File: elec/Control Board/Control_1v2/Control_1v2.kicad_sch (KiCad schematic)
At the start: 163 parts, among them J1 DB9_Female_MountingHoles, J10 Conn_02x12_Odd_Even, J11 Screw_Terminal_01x02, J14 Conn_01x10, J2 Conn_01x08, J25 Screw_Terminal_01x02, J26 Conn_01x10, J27 Conn_02x12_Odd_Even, J28 Screw_Terminal_01x02, J29 Conn_01x10, J3 Conn_01x08, J37 Conn_01x04, J4 Conn_01x08, J5 Conn_01x08, J6 Conn_01x08, J7 Conn_01x10, J8 Conn_02x18_Odd_Even, J9 Conn_01x10, Q601 BSS138

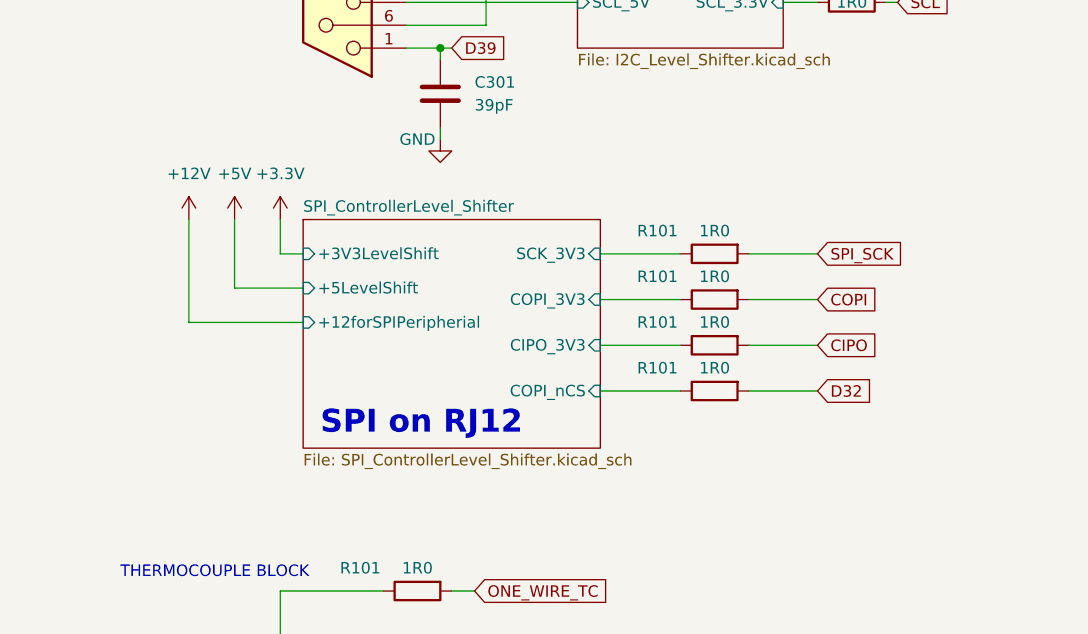
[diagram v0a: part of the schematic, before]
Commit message: Contrl 1.2 schematic, fix for Issue control board V1 kills ethernet boards #66
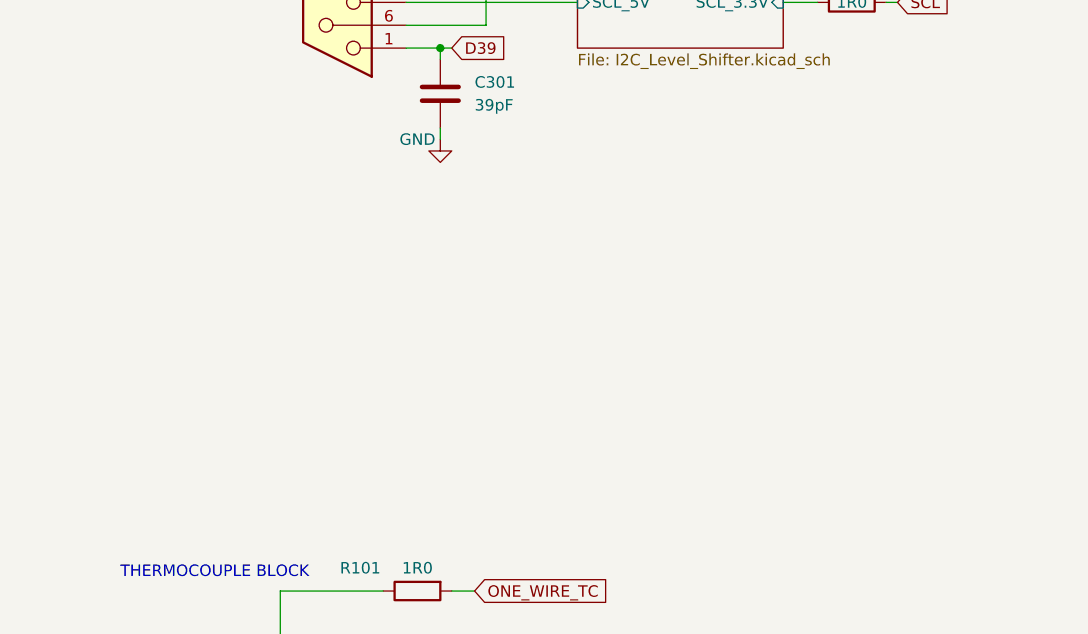
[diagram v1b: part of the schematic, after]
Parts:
- removed R101 (x4): 1R0, Resistor_SMD:R_0603_1608Metric_Pad0.98x0.95mm_HandSolder, symbol Device:R
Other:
- removed sheet SPI_ControllerLevel_Shifter
- note removed: "SPI on RJ12"

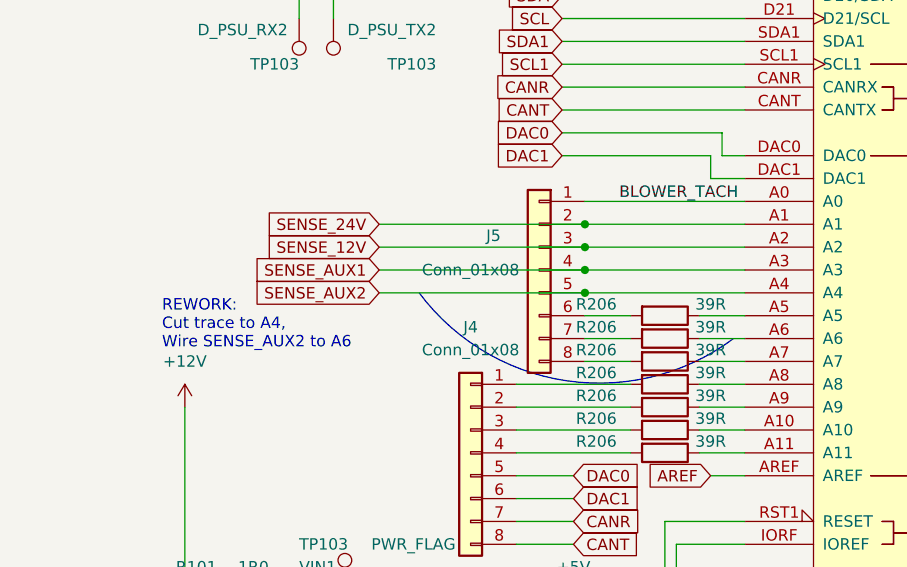
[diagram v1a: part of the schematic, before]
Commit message: Contrl 1.2 schematic, fix for Issue Control V1.1, A4 SENSE_AUX2 Conflicts With LAN Card SDA ( So does A5) #116
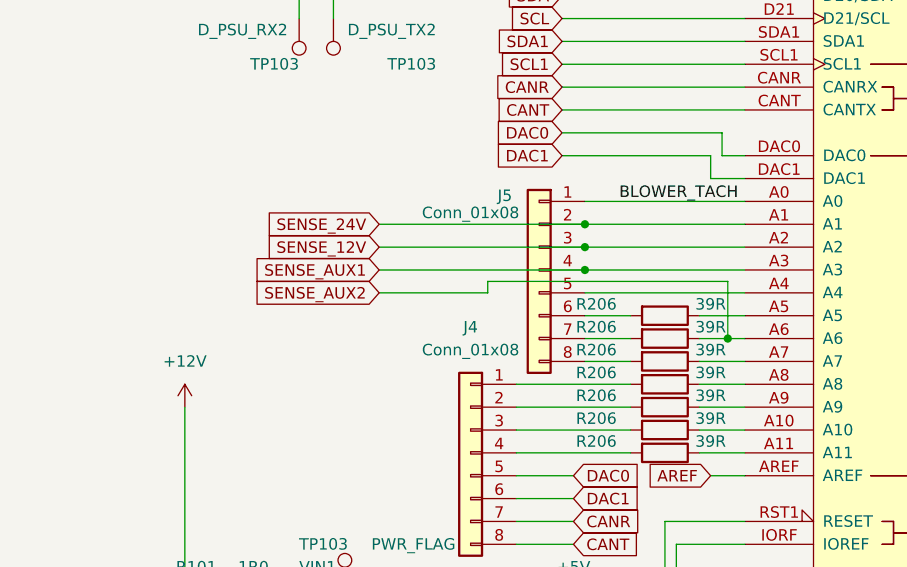
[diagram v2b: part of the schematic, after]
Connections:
- net SENSE_AUX2: now also A1.A6, R206.1; no longer A1.A4, J5.5 (Pin_5)
- new net: A1.A4, J5.5 (Pin_5)
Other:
- note removed: "REWORK: Cut trace to A4, Wire SENSE_AUX2 to A6"
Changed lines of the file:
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@@
   (junction (at 172.72 152.4) (diameter 0) (color 0 0 0 0)
   )
+  (junction (at 215.265 124.46) (diameter 0) (color 0 0 0 0)
+  )
   (junction (at 433.07 129.54) (diameter 0) (color 0 0 0 0)
   )
@@
   (junction (at 433.07 49.53) (diameter 0) (color 0 0 0 0)
   )
-  (junction (at 199.39 119.38) (diameter 0) (color 0 0 0 0)
-  )
   (junction (at 297.18 165.1) (diameter 0) (color 0 0 0 0)
   )
@@
     (stroke (width 0) (type default))
   )
+  (wire (pts (xy 215.265 124.46) (xy 217.17 124.46))
+    (stroke (width 0) (type default))
+  )
   (wire (pts (xy 463.55 148.59) (xy 463.55 134.62))
     (stroke (width 0) (type default))
@@
     (stroke (width 0) (type default))
   )
-  (wire (pts (xy 212.09 124.46) (xy 217.17 124.46))
-    (stroke (width 0) (type default))
-  )
   (wire (pts (xy 431.8 40.64) (xy 424.18 40.64))
     (stroke (width 0) (type default))
@@
     (stroke (width 0) (type default))
   )
+  (wire (pts (xy 188.595 118.11) (xy 188.595 119.38))
+    (stroke (width 0) (type default))
+  )
   (wire (pts (xy 307.34 139.7) (xy 317.5 139.7))
     (stroke (width 0) (type default))
@@
     (stroke (width 0) (type default))
   )
+  (wire (pts (xy 188.595 119.38) (xy 176.53 119.38))
+    (stroke (width 0) (type default))
+  )
   (wire (pts (xy 204.47 162.56) (xy 217.17 162.56))
     (stroke (width 0) (type default))
@@
     (stroke (width 0) (type default))
   )
+  (wire (pts (xy 212.09 124.46) (xy 215.265 124.46))
+    (stroke (width 0) (type default))
+  )
   (wire (pts (xy 488.95 261.62) (xy 494.03 261.62))
     (stroke (width 0) (type default))
@@
     (stroke (width 0) (type default))
   )
-  (wire (pts (xy 176.53 119.38) (xy 199.39 119.38))
-    (stroke (width 0) (type default))
-  )
   (wire (pts (xy 354.33 217.17) (xy 358.14 217.17))
     (stroke (width 0) (type default))
@@
     (stroke (width 0) (type default))
   )
+  (wire (pts (xy 199.39 124.46) (xy 204.47 124.46))
+    (stroke (width 0) (type default))
+  )
   (wire (pts (xy 199.39 119.38) (xy 217.17 119.38))
     (stroke (width 0) (type default))
@@
     (stroke (width 0) (type default))
   )
+  (wire (pts (xy 215.265 118.11) (xy 188.595 118.11))
+    (stroke (width 0) (type default))
+  )
   (wire (pts (xy 60.96 170.815) (xy 41.91 170.815))
     (stroke (width 0) (type default))
@@
     (stroke (width 0) (type default))
   )
+  (wire (pts (xy 215.265 124.46) (xy 215.265 118.11))
+    (stroke (width 0) (type default))
+  )
   (wire (pts (xy 161.29 45.72) (xy 161.29 52.07))
     (stroke (width 0) (type default))
@@
     (stroke (width 0) (type default))
   )
-  (wire (pts (xy 199.39 124.46) (xy 204.47 124.46))
-    (stroke (width 0) (type default))
-  )
   (wire (pts (xy 307.34 127) (xy 307.34 139.7))
     (stroke (width 0) (type default))
@@
     (fill (type none))
   )
-  (arc (start 215.9 124.46) (mid 197.3854 129.1532) (end 180.975 119.38)
-    (stroke (width 0) (type default))
-    (fill (type none))
-  )
   (arc (start 465.455 194.31) (mid 464.2381 204.8523) (end 455.93 211.455)
     (stroke (width 0) (type default))
@@
     (effects (font (size 1.27 1.27)) (justify left bottom))
   )
-  (text "REWORK:\nCut trace to A4,\nWire SENSE_AUX2 to A6" (at 152.4 125.73 0)
-    (effects (font (size 1.27 1.27)) (justify left bottom))
-  )
   (text "Blower Controller Signals\nFAN_POWER the Due output sets high to enable power to the blower.\nFAN1_FG is the Due input gets tachometer signal. Two low going edeges per revoluion.\nnFan1_PWM is negative aserted PWM to control blower speed."
     (at 302.26 189.23 0)
@@
   (symbol (lib_id "Connector_Generic:Conn_01x08") (at 194.31 116.84 0) (mirror y) (unit 1)
     (in_bom yes) (on_board yes) (dnp no)
-    (property "Reference" "J5" (at 189.23 113.03 0)
+    (property "Reference" "J5" (at 190.5 108.585 0)
       (effects (font (size 1.27 1.27)))
     )
-    (property "Value" "Conn_01x08" (at 186.69 116.84 0)
+    (property "Value" "Conn_01x08" (at 186.69 110.49 0)
       (effects (font (size 1.27 1.27)))
     )

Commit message: Contrl 1.2 schematic, fix for Issue: [200~Add TP to 5VHead, 5V, Change TP Values for SilkScreen
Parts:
- added TP103: 5VHead, TestPoint:TestPoint_Loop_D2.54mm_Drill1.5mm_Beaded, symbol Connector:TestPoint
- added TP103: +3.3V, TestPoint:TestPoint_Loop_D2.54mm_Drill1.5mm_Beaded, symbol Connector:TestPoint
- added TP103: +5V, TestPoint:TestPoint_Loop_D2.54mm_Drill1.5mm_Beaded, symbol Connector:TestPoint
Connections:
- net +3.3V: now also TP103.1
- net +5V: now also TP103.1
- net 5VHead: now also TP103.1
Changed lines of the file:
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@@
   (junction (at 257.81 34.29) (diameter 0) (color 0 0 0 0)
   )
+  (junction (at 209.55 182.88) (diameter 0) (color 0 0 0 0)
+  )
   (junction (at 509.27 53.34) (diameter 0) (color 0 0 0 0)
   )
@@
   (junction (at 81.28 53.34) (diameter 0) (color 0 0 0 0)
   )
+  (junction (at 190.5 181.61) (diameter 0) (color 0 0 0 0)
+  )
   (junction (at 181.61 152.4) (diameter 0) (color 0 0 0 0)
   )
@@
   (junction (at 201.93 71.12) (diameter 0) (color 0 0 0 0)
   )
+  (junction (at 180.34 184.15) (diameter 0) (color 0 0 0 0)
+  )
   (junction (at 64.135 296.545) (diameter 0) (color 0 0 0 0)
   )
@@
     (stroke (width 0) (type default))
   )
-  (wire (pts (xy 185.42 184.15) (xy 167.64 184.15))
+  (wire (pts (xy 185.42 184.15) (xy 180.34 184.15))
     (stroke (width 0) (type default))
   )
@@
     (stroke (width 0) (type default))
   )
+  (wire (pts (xy 190.5 165.1) (xy 190.5 181.61))
+    (stroke (width 0) (type default))
+  )
   (wire (pts (xy 76.2 80.01) (xy 76.2 81.28))
     (stroke (width 0) (type default))
@@
     (stroke (width 0) (type default))
   )
-  (wire (pts (xy 190.5 165.1) (xy 190.5 176.53))
-    (stroke (width 0) (type default))
-  )
   (wire (pts (xy 438.15 202.565) (xy 438.15 206.375))
     (stroke (width 0) (type default))
@@
     (stroke (width 0) (type default))
   )
+  (wire (pts (xy 190.5 181.61) (xy 190.5 186.69))
+    (stroke (width 0) (type default))
+  )
   (wire (pts (xy 283.21 91.44) (xy 288.29 91.44))
     (stroke (width 0) (type default))
@@
     (stroke (width 0) (type default))
   )
+  (wire (pts (xy 209.55 182.88) (xy 209.55 187.325))
+    (stroke (width 0) (type default))
+  )
   (wire (pts (xy 172.72 152.4) (xy 181.61 152.4))
     (stroke (width 0) (type default))
@@
     (stroke (width 0) (type default))
   )
+  (wire (pts (xy 180.34 184.15) (xy 180.34 186.69))
+    (stroke (width 0) (type default))
+  )
   (wire (pts (xy 209.55 176.53) (xy 210.82 176.53))
     (stroke (width 0) (type default))
   )
+  (wire (pts (xy 180.34 184.15) (xy 167.64 184.15))
+    (stroke (width 0) (type default))
+  )
   (wire (pts (xy 154.94 152.4) (xy 158.75 152.4))
     (stroke (width 0) (type default))
@@
     )
   )
+  (symbol (lib_id "Connector:TestPoint") (at 209.55 187.325 180) (unit 1)
+    (in_bom yes) (on_board yes) (dnp no)
+    (property "Reference" "TP103" (at 217.17 192.405 0)
+      (effects (font (size 1.27 1.27)) (justify left))
+    )
+    (property "Value" "5VHead" (at 217.805 190.5 0)
+      (effects (font (size 1.27 1.27)) (justify left))
+    )
+    (property "Footprint" "TestPoint:TestPoint_Loop_D2.54mm_Drill1.5mm_Beaded" (at 204.47 187.325 0)
+      (effects (font (size 1.27 1.27)) hide)
+    )
+    (property "Datasheet" "~" (at 204.47 187.325 0)
+      (effects (font (size 1.27 1.27)) hide)
+    )
+    (property "AssemblyType" "HAND" (at 209.55 187.325 0)
+      (effects (font (size 1.27 1.27)) hide)
+    )
+    (property "Cost" "0" (at 209.55 187.325 0)
+      (effects (font (size 1.27 1.27)) hide)
+    )
+    (pin "1")
+    (instances
+      (project "GeneralPurposeAlarmDevicePCB"
+        (path "/412a327d-1ee3-473e-bc00-1545004b7edf"
+          (reference "TP103") (unit 1)
+        )
+      )
+      (project "Control_1v2"
+        (path "/c68c9deb-8d4d-42f0-adf8-4d3022f4ee59/3ff32a52-b1ed-4756-8661-90a95f721605"
+          (reference "TP1") (unit 1)
+        )
+        (path "/c68c9deb-8d4d-42f0-adf8-4d3022f4ee59"
+          (reference "5VHead") (unit 1)
+        )
+      )
+    )
+  )
   (symbol (lib_id "Device:R") (at 292.1 101.6 270) (unit 1)
     (in_bom yes) (on_board yes) (dnp no)
@@
   )
   (symbol (lib_id "power:PWR_FLAG") (at 205.74 182.88 180) (unit 1)
-    (in_bom yes) (on_board yes) (dnp no) (fields_autoplaced)
+    (in_bom yes) (on_board yes) (dnp no)
     (property "Reference" "#FLG02" (at 205.74 184.785 0)
       (effects (font (size 1.27 1.27)) hide)
     )
-    (property "Value" "PWR_FLAG" (at 205.74 187.96 0)
+    (property "Value" "PWR_FLAG" (at 201.295 186.69 0)
       (effects (font (size 1.27 1.27)))
     )
@@
     )
   )
+  (symbol (lib_id "Connector:TestPoint") (at 180.34 186.69 180) (unit 1)
+    (in_bom yes) (on_board yes) (dnp no)
+    (property "Reference" "TP103" (at 186.69 191.135 0)
+      (effects (font (size 1.27 1.27)) (justify left))
+    )
+    (property "Value" "+3.3V" (at 186.69 189.23 0)
+      (effects (font (size 1.27 1.27)) (justify left))
+    )
+    (property "Footprint" "TestPoint:TestPoint_Loop_D2.54mm_Drill1.5mm_Beaded" (at 175.26 186.69 0)
+      (effects (font (size 1.27 1.27)) hide)
+    )
+    (property "Datasheet" "~" (at 175.26 186.69 0)
+      (effects (font (size 1.27 1.27)) hide)
+    )
+    (property "AssemblyType" "HAND" (at 180.34 186.69 0)
+      (effects (font (size 1.27 1.27)) hide)
+    )
+    (property "Cost" "0" (at 180.34 186.69 0)
+      (effects (font (size 1.27 1.27)) hide)
+    )
+    (pin "1")
+    (instances
+      (project "GeneralPurposeAlarmDevicePCB"
+        (path "/412a327d-1ee3-473e-bc00-1545004b7edf"
+          (reference "TP103") (unit 1)
+        )
+      )
+      (project "Control_1v2"
+        (path "/c68c9deb-8d4d-42f0-adf8-4d3022f4ee59/3ff32a52-b1ed-4756-8661-90a95f721605"
+          (reference "TP1") (unit 1)
+        )
+        (path "/c68c9deb-8d4d-42f0-adf8-4d3022f4ee59"
+          (reference "+3.3V") (unit 1)
+        )
+      )
+    )
+  )
   (symbol (lib_id "Device:R") (at 487.68 148.59 270) (unit 1)
     (in_bom yes) (on_board yes) (dnp no)
@@
     )
   )
-  (symbol (lib_id "power:PWR_FLAG") (at 190.5 176.53 180) (unit 1)
+  (symbol (lib_id "power:PWR_FLAG") (at 190.5 181.61 270) (unit 1)
     (in_bom yes) (on_board yes) (dnp no) (fields_autoplaced)
-    (property "Reference" "#FLG01" (at 190.5 178.435 0)
+    (property "Reference" "#FLG01" (at 192.405 181.61 0)
       (effects (font (size 1.27 1.27)) hide)
     )
-    (property "Value" "PWR_FLAG" (at 190.5 181.61 0)
-      (effects (font (size 1.27 1.27)))
+    (property "Value" "PWR_FLAG" (at 194.31 181.61 90)
+      (effects (font (size 1.27 1.27)) (justify left))
     )
-    (property "Footprint" "" (at 190.5 176.53 0)
+    (property "Footprint" "" (at 190.5 181.61 0)
       (effects (font (size 1.27 1.27)) hide)
     )
-    (property "Datasheet" "~" (at 190.5 176.53 0)
+    (property "Datasheet" "~" (at 190.5 181.61 0)
       (effects (font (size 1.27 1.27)) hide)
     )
@@
         )
       )
+    )
+  )
+  (symbol (lib_id "Connector:TestPoint") (at 190.5 186.69 180) (unit 1)
+    (in_bom yes) (on_board yes) (dnp no)
+    (property "Reference" "TP103" (at 194.945 191.135 0)
+      (effects (font (size 1.27 1.27)) (justify left))
+    )
+    (property "Value" "+5V" (at 194.945 189.23 0)
+      (effects (font (size 1.27 1.27)) (justify left))
+    )
+    (property "Footprint" "TestPoint:TestPoint_Loop_D2.54mm_Drill1.5mm_Beaded" (at 185.42 186.69 0)
+      (effects (font (size 1.27 1.27)) hide)
+    )
+    (property "Datasheet" "~" (at 185.42 186.69 0)
+      (effects (font (size 1.27 1.27)) hide)
+    )
+    (property "AssemblyType" "HAND" (at 190.5 186.69 0)
+      (effects (font (size 1.27 1.27)) hide)
+    )
+    (property "Cost" "0" (at 190.5 186.69 0)
+      (effects (font (size 1.27 1.27)) hide)
+    )
+    (pin "1")
+    (instances
+      (project "GeneralPurposeAlarmDevicePCB"
+        (path "/412a327d-1ee3-473e-bc00-1545004b7edf"
+          (reference "TP103") (unit 1)
+        )
+      )
+      (project "Control_1v2"
+        (path "/c68c9deb-8d4d-42f0-adf8-4d3022f4ee59/3ff32a52-b1ed-4756-8661-90a95f721605"
+          (reference "TP1") (unit 1)
+        )
+        (path "/c68c9deb-8d4d-42f0-adf8-4d3022f4ee59"
+          (reference "+5V") (unit 1)
+        )
+      )

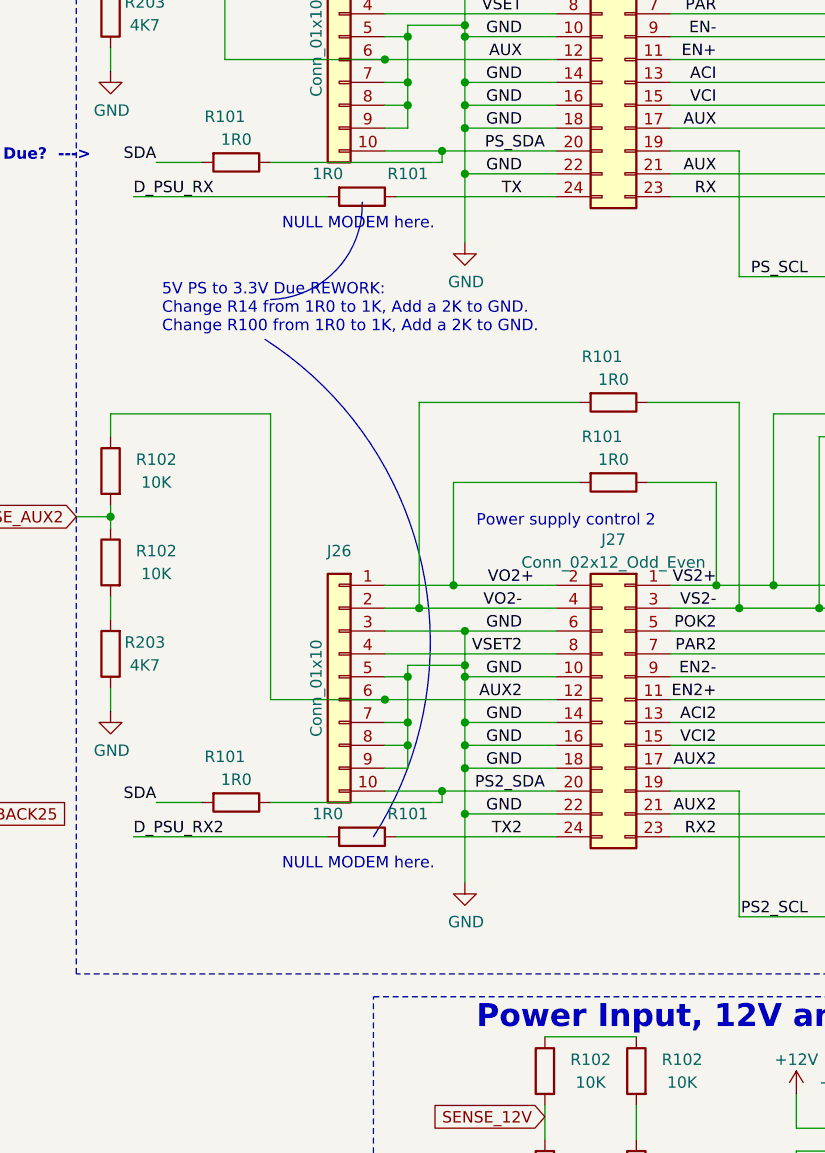
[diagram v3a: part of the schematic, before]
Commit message: Contrl 1.2 schematic, fix for Issue: hds800ps12 and TF800A12K appear to be 5v TTL logic, and not 3.3v #144
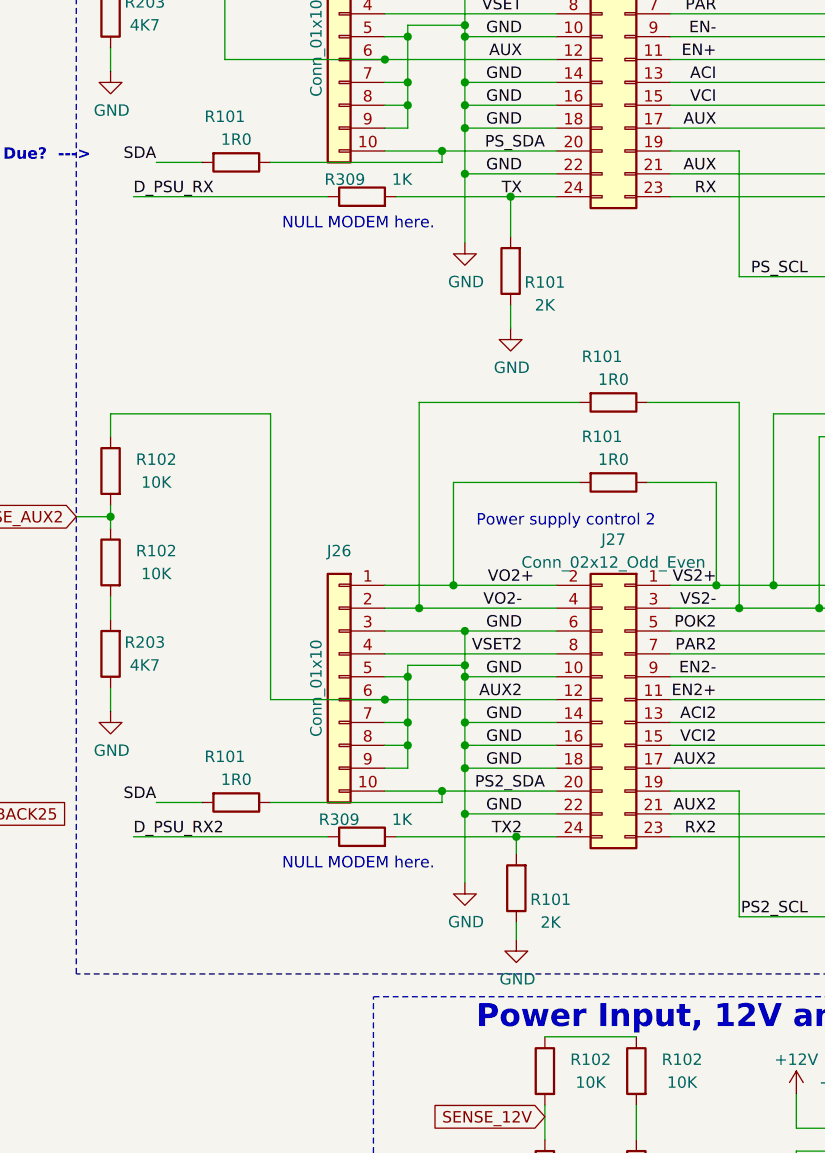
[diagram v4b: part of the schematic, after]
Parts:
- removed R101 (x2): 1R0, Resistor_SMD:R_0603_1608Metric_Pad0.98x0.95mm_HandSolder, symbol Device:R
- added R101 (x2): 2K, Resistor_SMD:R_0603_1608Metric_Pad0.98x0.95mm_HandSolder, symbol Device:R
- added R309 (x2): 1K, Resistor_SMD:R_0603_1608Metric_Pad0.98x0.95mm_HandSolder, symbol Device:R
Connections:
- net D_PSU_RX: now also R309.1
- net D_PSU_RX2: now also R309.1
- net GND: now also R101.1, R101.1
- net TX: now also R101.2, R309.2
- net TX2: now also R101.2, R309.2
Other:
- note removed: "5V PS to 3.3V Due REWORK: Change R14 from 1R0 to 1K, Add a 2K to GND. Change R100 from 1R0 to 1K, Add a 2K to GND."
